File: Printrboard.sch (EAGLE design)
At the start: 119 parts, among them J1 MICROSD, J2 USB-MICROB, J3 ATX, Q1 RFP30N06LE, Q2 RFP30N06LE, Q3 RFP30N06LE, U1 LM2841, U2 A4982, U3 A4982, U4 A4982, U5 A4982, U6 AT90USB1286, U7 AP7313, U8 TXB0104, X1 8MHz

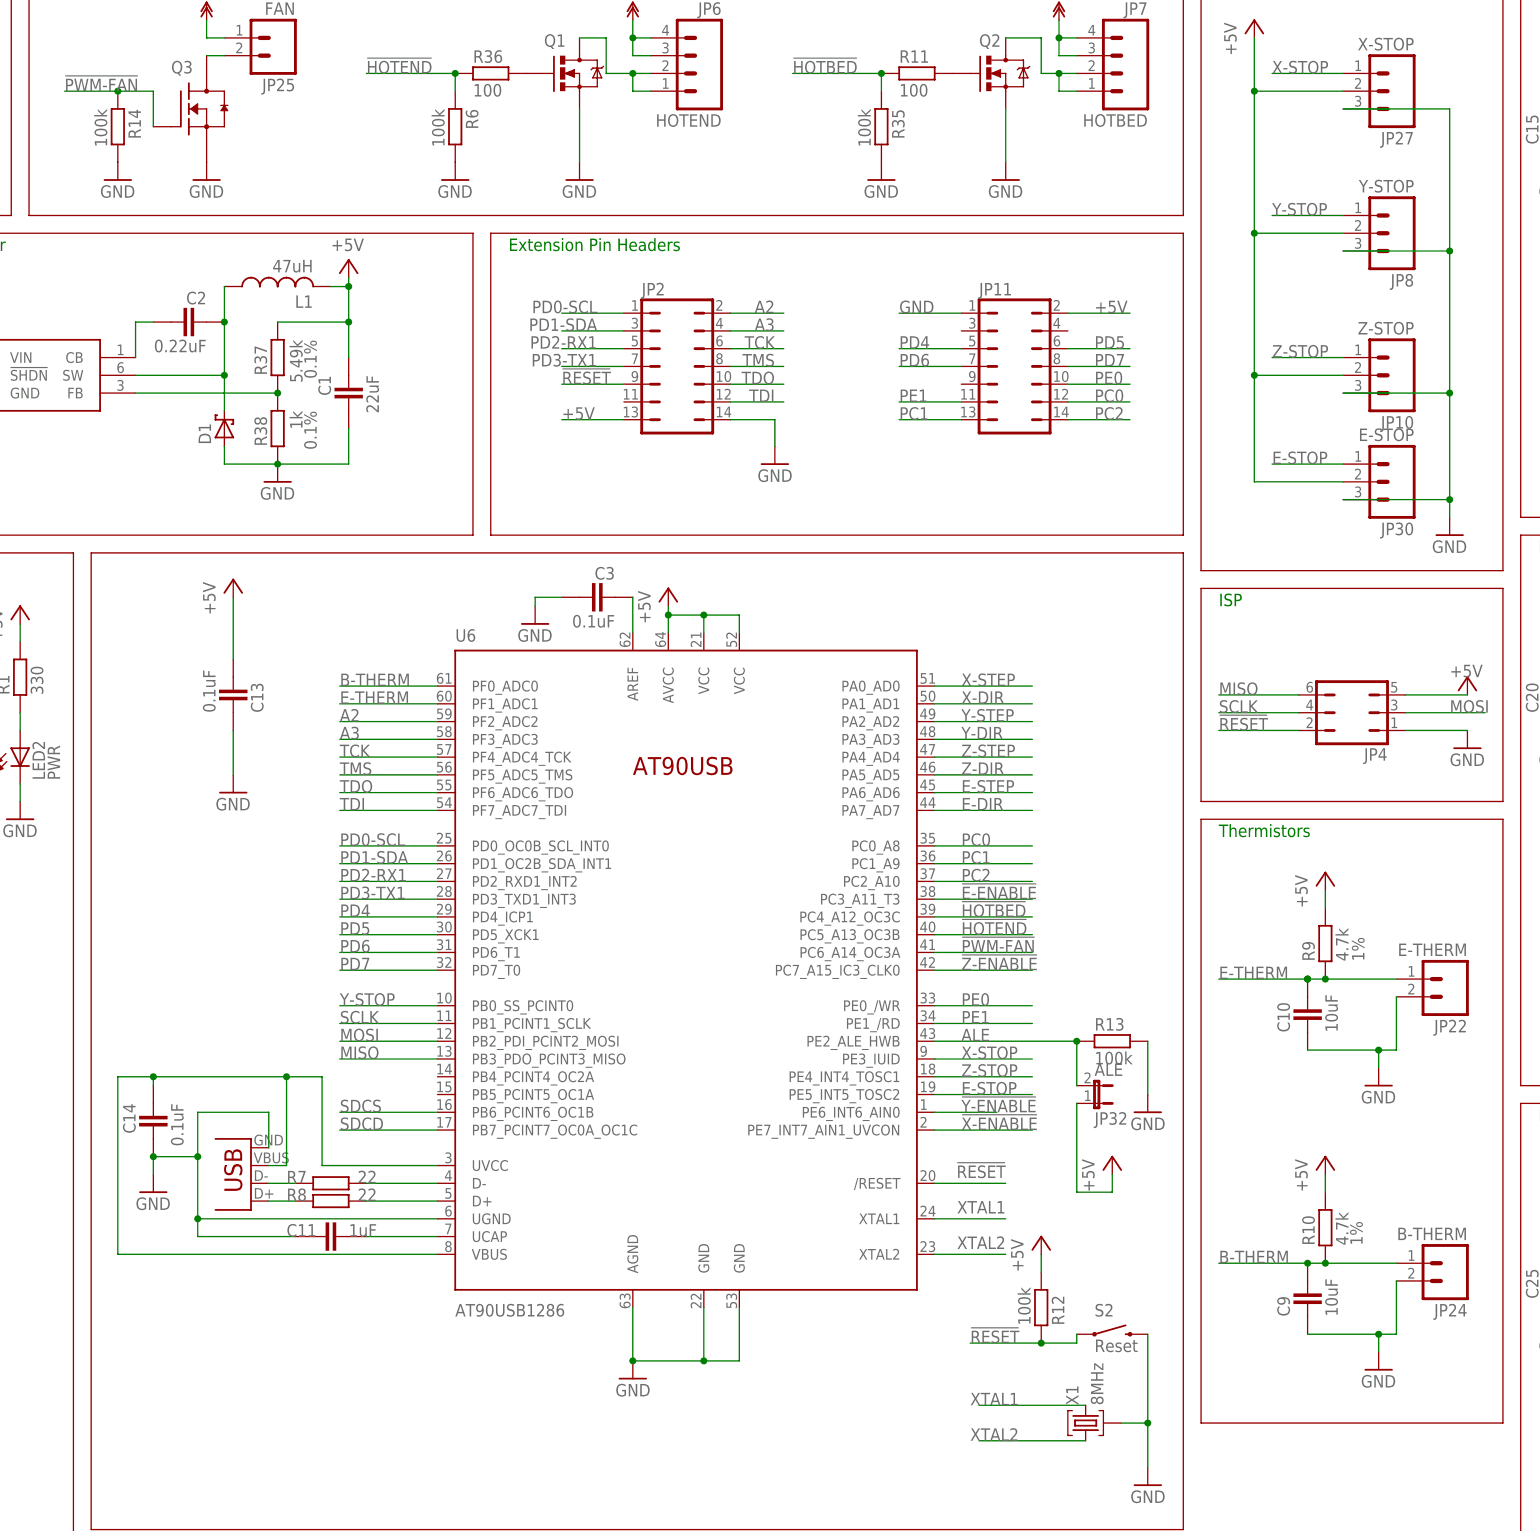
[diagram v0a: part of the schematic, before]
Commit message: Fix angle errors caused by 6.0 conversion, add more decoupling caps to MCU, and modify some routing
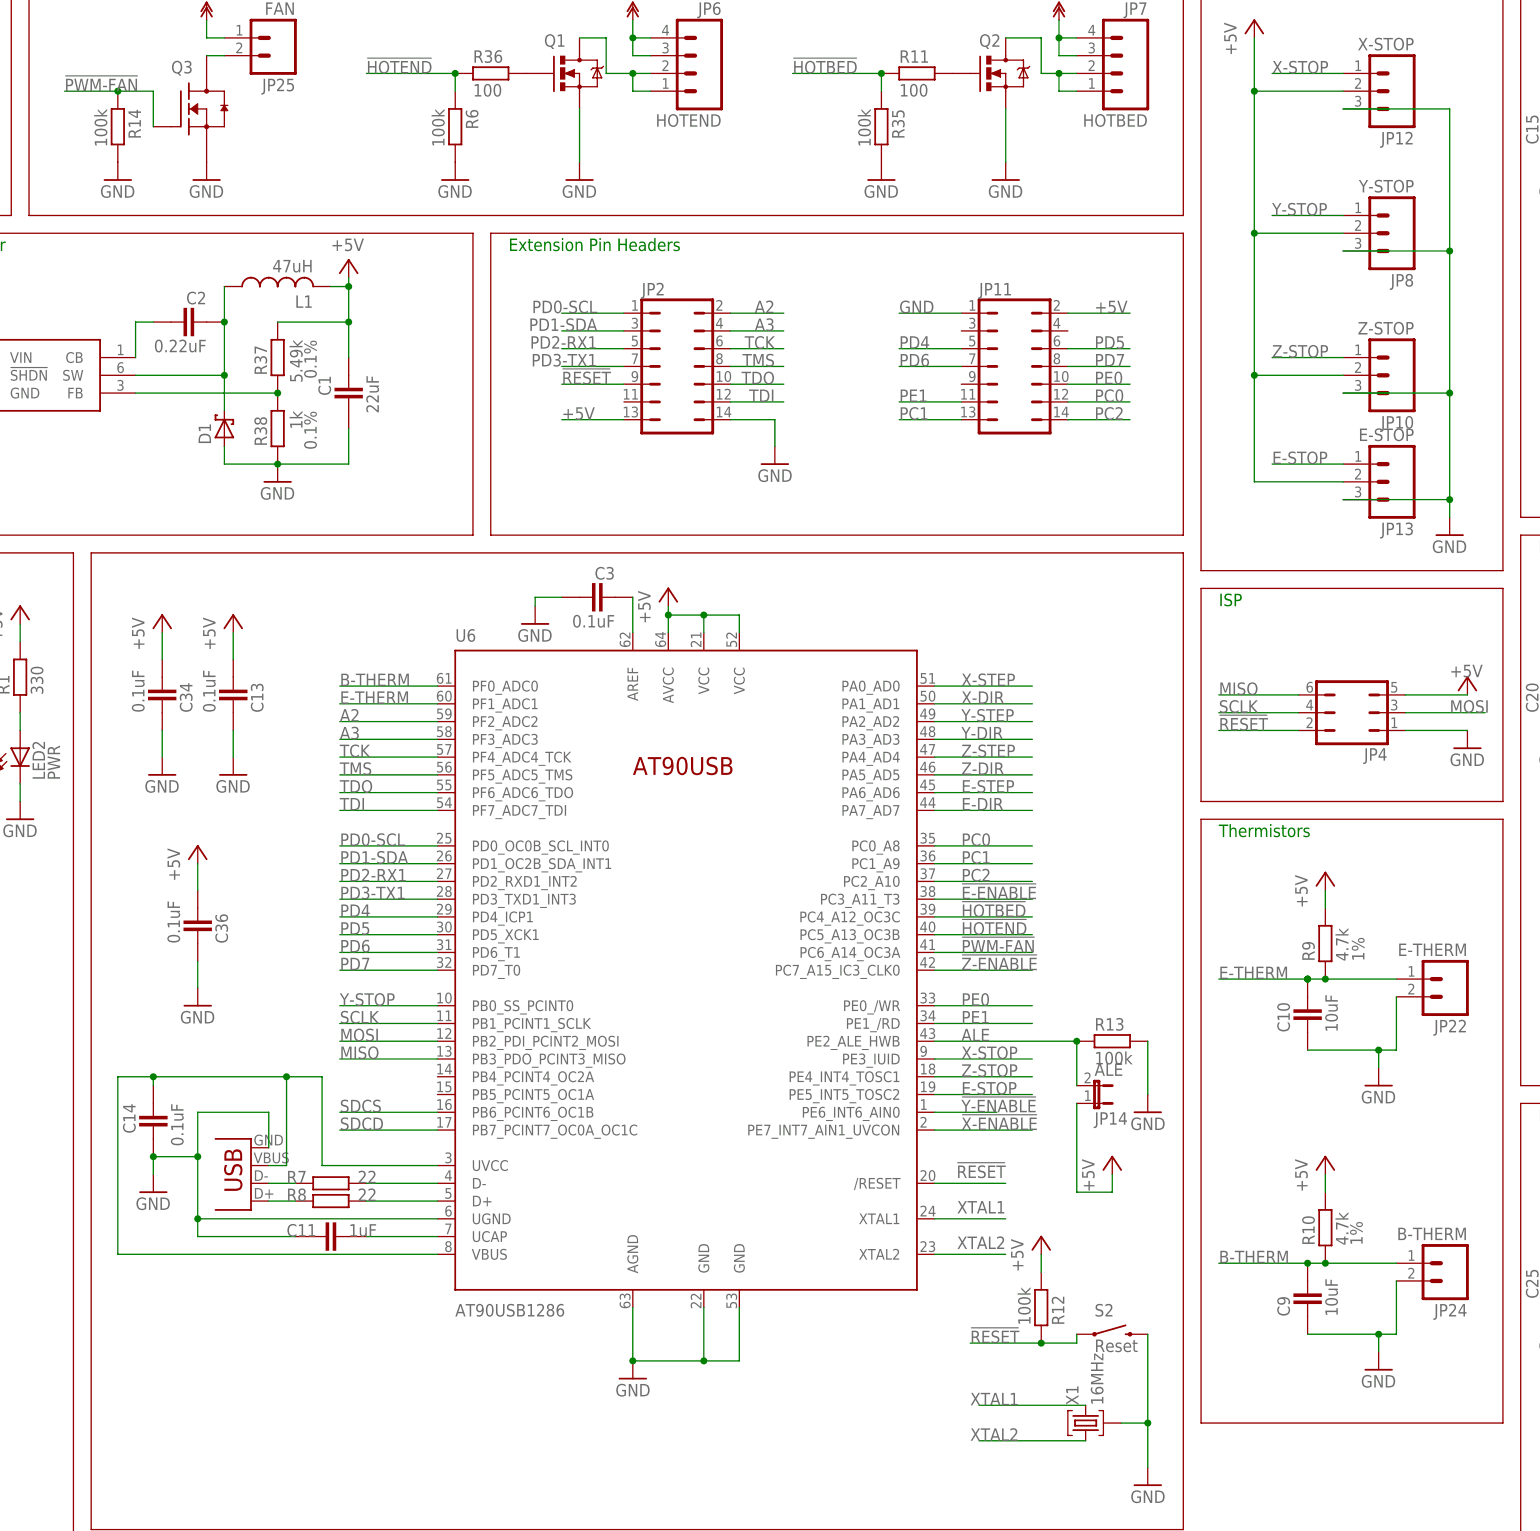
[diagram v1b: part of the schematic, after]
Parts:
- added C34, C36: 0.1uF, ipc-7351-capacitor:CAPACITOR_0805
- X1: value 8MHz -> 16MHz
- renumbered JP27 to JP12, JP30 to JP13, JP32 to JP14
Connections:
- net +5V: now also C34.2, C36.2
- net GND: now also C34.1, C36.1
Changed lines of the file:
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@@
 <setting verticaltext="up"/>
 </settings>
-<grid distance="0.1" unitdist="inch" unit="inch" style="lines" multiple="1" display="no" altdistance="0.05" altunitdist="inch" altunit="inch"/>
+<grid distance="0.1" unitdist="inch" unit="inch" style="lines" multiple="1" display="no" altdistance="0.01" altunitdist="inch" altunit="inch"/>
 <layers>
 <layer number="1" name="Top" color="4" fill="1" visible="no" active="no"/>
@@
 </part>
 <part name="GND27" library="supply1" deviceset="GND" device=""/>
-<part name="JP27" library="SparkFun" deviceset="M03" device="POLAR" value="X-STOP"/>
+<part name="JP12" library="SparkFun" deviceset="M03" device="POLAR" value="X-STOP"/>
 <part name="Q1" library="SparkFun" deviceset="MOSFET-NCHANNEL" device="PTH2" value="RFP30N06LE"/>
 <part name="Q2" library="SparkFun" deviceset="MOSFET-NCHANNEL" device="PTH2" value="RFP30N06LE"/>
@@
 <part name="C11" library="ipc-7351-capacitor" deviceset="CAPACITOR_" device="0805" value="1uF"/>
 <part name="R13" library="ipc-7351-resistor" deviceset="RESISTOR_" device="0805" value="100k"/>
-<part name="JP30" library="SparkFun" deviceset="M03" device="POLAR" value="E-STOP"/>
+<part name="JP13" library="SparkFun" deviceset="M03" device="POLAR" value="E-STOP"/>
 <part name="C9" library="ipc-7351-capacitor" deviceset="CAPACITOR_" device="0805" value="10uF"/>
 <part name="C10" library="ipc-7351-capacitor" deviceset="CAPACITOR_" device="0805" value="10uF"/>
@@
 <part name="JP25" library="SparkFun" deviceset="M02" device="PTH" value="FAN"/>
 <part name="U$38" library="12v" deviceset="12V" device=""/>
-<part name="JP32" library="SparkFun" deviceset="JUMPER-2" device="PTH" value="ALE"/>
+<part name="JP14" library="SparkFun" deviceset="JUMPER-2" device="PTH" value="ALE"/>
 <part name="R1" library="ipc-7351-resistor" deviceset="RESISTOR_" device="0805" value="330"/>
 <part name="S2" library="SparkFun" deviceset="SWITCH-MOMENTARY-2" device="" value="Reset"/>
@@
 <part name="GND15" library="SparkFun" deviceset="GND" device=""/>
 <part name="U$5" library="12v" deviceset="12V" device=""/>
-<part name="X1" library="printrbot" deviceset="AWSCR-CV" device="" value="8MHz"/>
+<part name="X1" library="printrbot" deviceset="AWSCR-CV" device="" value="16MHz"/>
 <part name="GND19" library="SparkFun" deviceset="GND" device=""/>
 <part name="C6" library="rcl" deviceset="CPOL-US" device="D" value="100uF"/>
@@
 <part name="JP11" library="printrbot" deviceset="JP7Q" device=""/>
 <part name="JP4" library="printrbot" deviceset="JP3Q" device=""/>
+<part name="C34" library="ipc-7351-capacitor" deviceset="CAPACITOR_" device="0805" value="0.1uF"/>
+<part name="GND50" library="SparkFun" deviceset="GND" device=""/>
+<part name="P+17" library="supply1" deviceset="+5V" device=""/>
+<part name="C36" library="ipc-7351-capacitor" deviceset="CAPACITOR_" device="0805" value="0.1uF"/>
+<part name="GND51" library="SparkFun" deviceset="GND" device=""/>
+<part name="P+18" library="supply1" deviceset="+5V" device=""/>
 </parts>
 <sheets>
@@
 </instance>
 <instance part="GND27" gate="1" x="231.14" y="160.02"/>
-<instance part="JP27" gate="G$1" x="223.52" y="223.52" rot="R180"/>
+<instance part="JP12" gate="G$1" x="223.52" y="223.52" rot="R180"/>
 <instance part="Q1" gate="G$1" x="106.68" y="226.06" smashed="yes">
 <attribute name="NAME" x="101.6" y="229.87" size="1.778" layer="95"/>
@@
 </instance>
 <instance part="R13" gate="G$1" x="182.88" y="87.63"/>
-<instance part="JP30" gate="G$1" x="223.52" y="167.64" rot="R180"/>
+<instance part="JP13" gate="G$1" x="223.52" y="167.64" rot="R180"/>
 <instance part="C9" gate="G$1" x="210.82" y="50.8" rot="R90"/>
 <instance part="C10" gate="G$1" x="210.82" y="91.44" rot="R90"/>
-<instance part="GND5" gate="1" x="57.15" y="123.19"/>
+<instance part="GND5" gate="1" x="57.15" y="125.73"/>
 <instance part="GND14" gate="1" x="26.67" y="119.38"/>
 <instance part="JP26" gate="G$1" x="176.53" y="12.7"/>
@@
 <instance part="JP25" gate="G$1" x="63.5" y="231.14" rot="R180"/>
 <instance part="U$38" gate="G$1" x="53.34" y="233.68"/>
-<instance part="JP32" gate="A" x="180.34" y="78.74" rot="MR90"/>
+<instance part="JP14" gate="A" x="180.34" y="78.74" rot="MR90"/>
 <instance part="R1" gate="G$1" x="26.67" y="139.7" rot="R90"/>
 <instance part="S2" gate="G$1" x="182.88" y="45.72"/>
@@
 <instance part="C32" gate="G$1" x="90.17" y="-45.72" rot="MR270"/>
 <instance part="P+1" gate="1" x="119.38" y="152.4"/>
-<instance part="P+2" gate="1" x="57.15" y="153.67"/>
+<instance part="P+2" gate="1" x="57.15" y="148.59"/>
 <instance part="P+3" gate="1" x="26.67" y="149.86"/>
 <instance part="P+4" gate="1" x="73.66" y="199.39" smashed="yes">
@@
 <instance part="JP11" gate="B" x="168.91" y="184.15" rot="R270"/>
 <instance part="JP4" gate="B" x="217.17" y="134.62" rot="R90"/>
+<instance part="C34" gate="G$1" x="46.99" y="137.16" rot="MR90"/>
+<instance part="GND50" gate="1" x="46.99" y="125.73"/>
+<instance part="P+17" gate="1" x="46.99" y="148.59"/>
+<instance part="C36" gate="G$1" x="52.07" y="104.14" rot="MR90"/>
+<instance part="GND51" gate="1" x="52.07" y="92.71"/>
+<instance part="P+18" gate="1" x="52.07" y="115.57"/>
 </instances>
 <busses>
@@
 <junction x="231.14" y="180.34"/>
 <junction x="231.14" y="165.1"/>
-<pinref part="JP27" gate="G$1" pin="3"/>
+<pinref part="JP12" gate="G$1" pin="3"/>
 <pinref part="GND27" gate="1" pin="GND"/>
-<pinref part="JP30" gate="G$1" pin="3"/>
+<pinref part="JP13" gate="G$1" pin="3"/>
 <pinref part="JP8" gate="G$1" pin="3"/>
 <pinref part="JP10" gate="G$1" pin="3"/>
@@
 </segment>
 <segment>
-<wire x1="57.15" y1="125.73" x2="57.15" y2="132.08" width="0.1524" layer="91"/>
+<wire x1="57.15" y1="128.27" x2="57.15" y2="132.08" width="0.1524" layer="91"/>
 <pinref part="GND5" gate="1" pin="GND"/>
 <pinref part="C13" gate="G$1" pin="1"/>
@@
 <pinref part="GND49" gate="1" pin="GND"/>
 </segment>
+<segment>
+<wire x1="46.99" y1="128.27" x2="46.99" y2="132.08" width="0.1524" layer="91"/>
+<pinref part="GND50" gate="1" pin="GND"/>
+<pinref part="C34" gate="G$1" pin="1"/>
+</segment>
+<segment>
+<wire x1="52.07" y1="95.25" x2="52.07" y2="99.06" width="0.1524" layer="91"/>
+<pinref part="GND51" gate="1" pin="GND"/>
+<pinref part="C36" gate="G$1" pin="1"/>
+</segment>
 </net>
 <net name="!RESET" class="0">
@@
 <wire x1="215.9" y1="226.06" x2="205.74" y2="226.06" width="0.1524" layer="91"/>
 <label x="205.74" y="226.06" size="1.778" layer="95"/>
-<pinref part="JP27" gate="G$1" pin="1"/>
+<pinref part="JP12" gate="G$1" pin="1"/>
 </segment>
 <segment>
@@
 <wire x1="215.9" y1="170.18" x2="205.74" y2="170.18" width="0.1524" layer="91"/>
 <label x="205.74" y="170.18" size="1.778" layer="95"/>
-<pinref part="JP30" gate="G$1" pin="1"/>
+<pinref part="JP13" gate="G$1" pin="1"/>
 </segment>
 <segment>
@@
 <pinref part="R13" gate="G$1" pin="1"/>
 <pinref part="U6" gate="G$1" pin="PE2_ALE_HWB"/>
-<pinref part="JP32" gate="A" pin="2"/>
+<pinref part="JP14" gate="A" pin="2"/>
 </segment>
 </net>
@@
 </segment>
 <segment>
-<wire x1="57.15" y1="151.13" x2="57.15" y2="142.24" width="0.1524" layer="91"/>
+<wire x1="57.15" y1="146.05" x2="57.15" y2="142.24" width="0.1524" layer="91"/>
 <pinref part="C13" gate="G$1" pin="2"/>
 <pinref part="P+2" gate="1" pin="+5V"/>
@@
 <wire x1="177.8" y1="66.04" x2="182.88" y2="66.04" width="0.1524" layer="91"/>
 <wire x1="182.88" y1="66.04" x2="182.88" y2="68.58" width="0.1524" layer="91"/>
-<pinref part="JP32" gate="A" pin="1"/>
+<pinref part="JP14" gate="A" pin="1"/>
 <pinref part="P+6" gate="1" pin="+5V"/>
 </segment>
@@
 <junction x="203.2" y="182.88"/>
 <junction x="203.2" y="223.52"/>
-<pinref part="JP30" gate="G$1" pin="2"/>
-<pinref part="JP27" gate="G$1" pin="2"/>
+<pinref part="JP13" gate="G$1" pin="2"/>
+<pinref part="JP12" gate="G$1" pin="2"/>
 <pinref part="P+11" gate="1" pin="+5V"/>
 <pinref part="JP8" gate="G$1" pin="2"/>
@@
 <pinref part="JP11" gate="B" pin="2"/>
 </segment>
-</net>
+<segment>
+<wire x1="46.99" y1="146.05" x2="46.99" y2="142.24" width="0.1524" layer="91"/>
+<pinref part="C34" gate="G$1" pin="2"/>
+<pinref part="P+17" gate="1" pin="+5V"/>
+</segment>
+<segment>
+<wire x1="52.07" y1="113.03" x2="52.07" y2="109.22" width="0.1524" layer="91"/>
+<pinref part="C36" gate="G$1" pin="2"/>
+<pinref part="P+18" gate="1" pin="+5V"/>
+</segment>
+</net>
